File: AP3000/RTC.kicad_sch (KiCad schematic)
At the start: 10 parts, among them U14 74LVC1G07SE-7, U8 PCF85063AT/AAZ, Y2 X32K768S301

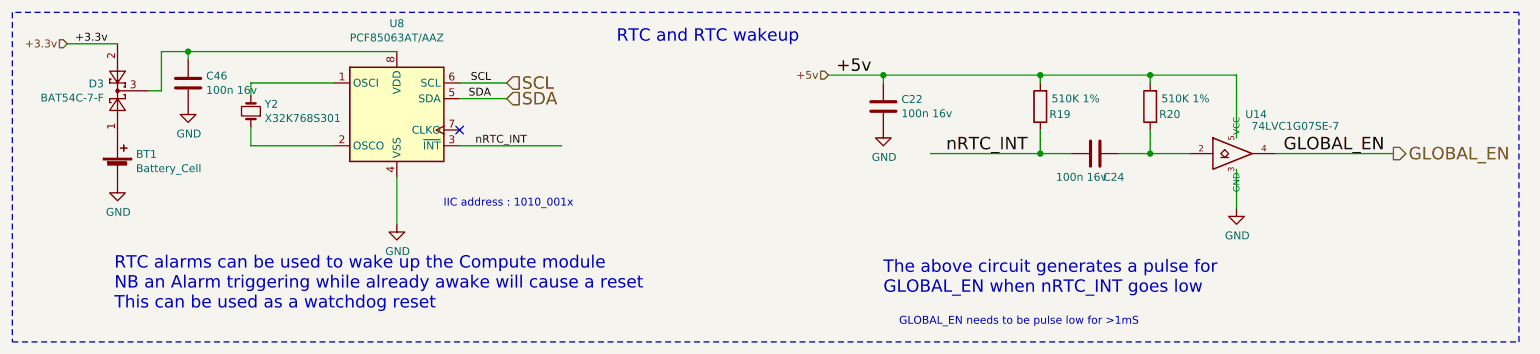
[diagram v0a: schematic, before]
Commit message: Update JLCPCB components for AP3000
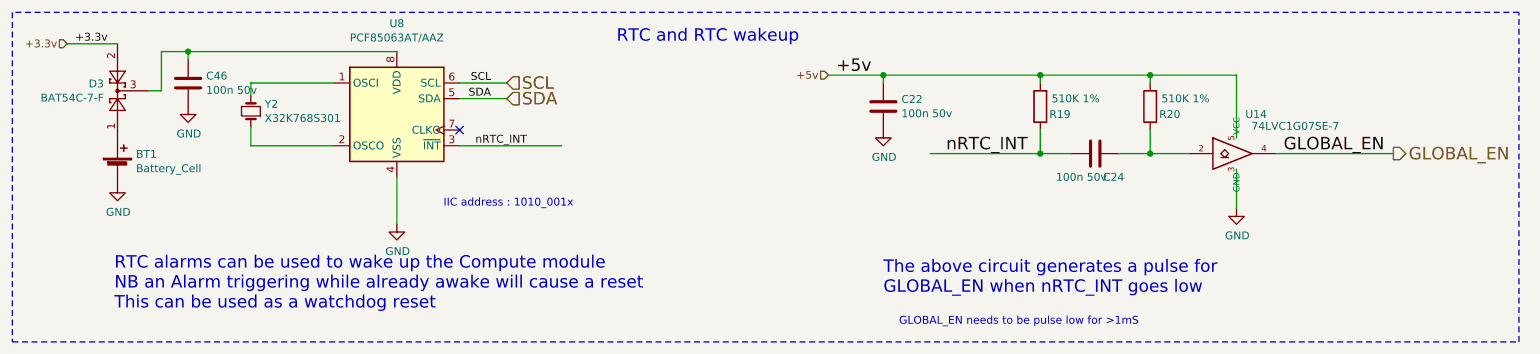
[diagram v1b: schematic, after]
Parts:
- BT1: Part Description Battery Retainer Coin, 20.0mm 1 Cell SMD (SMT) Tab -> Battery Retainer Coin, 20.0mm 1 Cell SMD (SMT) Tab
- C22, C24, C46: value 100n 16v -> 100n 50v; LCSC (none) -> C14663; Part Description 0.1uF 10% 16V Ceramic Capacitor X7R 0402 (1005 Metric) -> 100nF 10% or 20% 50V Ceramic Capacitor X7R 0603; PartsBoxID 0603-100nF-X7R-16V -> 0603-100nF-X7R-50V
- D3: LCSC (none) -> C134405
- R19, R20: LCSC (none) -> C23192
- U14: LCSC (none) -> C67531
- U8: LCSC (none) -> 2157792
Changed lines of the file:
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@@
       (effects (font (size 1.27 1.27)) hide)
     )
-    (property "PartsBoxID" "ABS07-32.768KHZ-7-T" (id 4) (at 67.818 55.372 0)
+    (property "PartsBoxID" "ABS07-32.768KHZ-7-T" (id 7) (at 67.818 55.372 0)
       (effects (font (size 1.27 1.27)) hide)
     )
@@
       (effects (font (size 1.27 1.27)) hide)
     )
-    (property "PartsBoxID" "0603-510K-1%" (id 4) (at 195.58 54.61 0)
+    (property "PartsBoxID" "0603-510K-1%" (id 9) (at 195.58 54.61 0)
+      (effects (font (size 1.27 1.27)) hide)
+    )
+    (property "LCSC" "C23192" (id 10) (at 195.58 54.61 0)
       (effects (font (size 1.27 1.27)) hide)
     )
@@
       (effects (font (size 1.27 1.27)) hide)
     )
-    (property "PartsBoxID" "0603-510K-1%" (id 4) (at 213.36 54.61 0)
+    (property "PartsBoxID" "0603-510K-1%" (id 9) (at 213.36 54.61 0)
+      (effects (font (size 1.27 1.27)) hide)
+    )
+    (property "LCSC" "C23192" (id 10) (at 213.36 54.61 0)
       (effects (font (size 1.27 1.27)) hide)
     )
@@
       (effects (font (size 1.27 1.27)) hide)
     )
-    (property "Part Description" "	Battery Retainer Coin, 20.0mm 1 Cell SMD (SMT) Tab" (id 8) (at 46.228 64.77 0)
-      (effects (font (size 1.27 1.27)) hide)
-    )
-    (property "PartsBoxID" "3034" (id 4) (at 46.228 64.77 0)
+    (property "Part Description" "Battery Retainer Coin, 20.0mm 1 Cell SMD (SMT) Tab" (id 8) (at 46.228 64.77 0)
+      (effects (font (size 1.27 1.27)) hide)
+    )
+    (property "PartsBoxID" "3034" (id 9) (at 46.228 64.77 0)
       (effects (font (size 1.27 1.27)) hide)
     )
@@
       (effects (font (size 1.27 1.27)) (justify left))
     )
-    (property "Value" "100n 16v" (id 1) (at 60.579 51.9684 0)
+    (property "Value" "100n 50v" (id 1) (at 60.579 51.9684 0)
       (effects (font (size 1.27 1.27)) (justify left))
     )
@@
       (effects (font (size 1.27 1.27)) hide)
     )
-    (property "Part Description" "	0.1uF 10% 16V Ceramic Capacitor X7R 0402 (1005 Metric)" (id 8) (at 57.658 50.8254 0)
+    (property "Part Description" "100nF 10% or 20% 50V Ceramic Capacitor X7R 0603" (id 8) (at 57.658 50.8254 0)
       (effects (font (size 1.27 1.27)) hide)
     )
@@
       (effects (font (size 1.27 1.27)) hide)
     )
-    (property "PartsBoxID" "0603-100nF-X7R-16V" (id 4) (at 57.658 50.8254 0)
+    (property "PartsBoxID" "0603-100nF-X7R-50V" (id 10) (at 57.658 50.8254 0)
+      (effects (font (size 1.27 1.27)) hide)
+    )
+    (property "LCSC" "C14663" (id 11) (at 57.658 50.8254 0)
       (effects (font (size 1.27 1.27)) hide)
     )
@@
       (effects (font (size 1.27 1.27)) (justify left))
     )
-    (property "Value" "100n 16v" (id 1) (at 173.101 55.753 0)
+    (property "Value" "100n 50v" (id 1) (at 173.101 55.753 0)
       (effects (font (size 1.27 1.27)) (justify left))
     )
@@
       (effects (font (size 1.27 1.27)) hide)
     )
-    (property "Part Description" "	0.1uF 10% 16V Ceramic Capacitor X7R 0402 (1005 Metric)" (id 8) (at 170.18 54.61 0)
+    (property "Part Description" "100nF 10% or 20% 50V Ceramic Capacitor X7R 0603" (id 8) (at 170.18 54.61 0)
       (effects (font (size 1.27 1.27)) hide)
     )
@@
       (effects (font (size 1.27 1.27)) hide)
     )
-    (property "PartsBoxID" "0603-100nF-X7R-16V" (id 4) (at 170.18 54.61 0)
+    (property "PartsBoxID" "0603-100nF-X7R-50V" (id 10) (at 170.18 54.61 0)
+      (effects (font (size 1.27 1.27)) hide)
+    )
+    (property "LCSC" "C14663" (id 11) (at 170.18 54.61 0)
       (effects (font (size 1.27 1.27)) hide)
     )
@@
       (effects (font (size 1.27 1.27)) (justify left))
     )
-    (property "Value" "100n 16v" (id 1) (at 198.12 66.04 90)
+    (property "Value" "100n 50v" (id 1) (at 198.12 66.04 90)
       (effects (font (size 1.27 1.27)) (justify left))
     )
@@
       (effects (font (size 1.27 1.27)) hide)
     )
-    (property "Part Description" "	0.1uF 10% 16V Ceramic Capacitor X7R 0402 (1005 Metric)" (id 8) (at 204.47 62.23 0)
+    (property "Part Description" "100nF 10% or 20% 50V Ceramic Capacitor X7R 0603" (id 8) (at 204.47 62.23 0)
       (effects (font (size 1.27 1.27)) hide)
     )
@@
       (effects (font (size 1.27 1.27)) hide)
     )
-    (property "PartsBoxID" "0603-100nF-X7R-16V" (id 4) (at 204.47 62.23 0)
-      (effects (font (size 1.27 1.27)) hide)
-    )
-    (pin "1")
-    (pin "2")
-  )
-  (symbol (lib_id "Diode:BAT54C") (at 46.228 52.07 90) (unit 1)
-    (in_bom yes) (on_board yes)
-    (property "Reference" "D3" (id 0) (at 44.0182 50.927 90)
-      (effects (font (size 1.27 1.27)) (justify left))
-    )
-    (property "Value" "BAT54C-7-F" (id 1) (at 44.0182 53.213 90)
-      (effects (font (size 1.27 1.27)) (justify left))
-    )
-    (property "Footprint" "Package_TO_SOT_SMD:SOT-23" (id 2) (at 43.053 50.165 0)
-      (effects (font (size 1.27 1.27)) (justify left) hide)
-    )
-    (property "Datasheet" "http://www.farnell.com/datasheets/2861240.pdf?_ga=2.129831176.54358802.1587372871-1787849031.1568210898&_gac=1.175311126.1587399424.EAIaIQobChMInOvF07P36AIVw7HtCh0NWwCeEAAYAyAAEgI0YfD_BwE" (id 3) (at 46.228 54.102 0)
-      (effects (font (size 1.27 1.27)) hide)
-    )
-    (property "Field4" "Farnell" (id 4) (at 46.228 52.07 0)
-      (effects (font (size 1.27 1.27)) hide)
-    )
-    (property "Field5" "2306010" (id 5) (at 46.228 52.07 0)
-      (effects (font (size 1.27 1.27)) hide)
-    )
-    (property "Field6" "BAT54C-7-F" (id 6) (at 46.228 52.07 0)
-      (effects (font (size 1.27 1.27)) hide)
-    )
-    (property "Field7" "Rohm" (id 7) (at 46.228 52.07 0)
-      (effects (font (size 1.27 1.27)) hide)
-    )
-    (property "Part Description" "Diode Array 1 Pair Common Cathode Schottky 30V 200mA (DC) Surface Mount TO-236-3, SC-59, SOT-23-3" (id 8) (at 46.228 52.07 0)
-      (effects (font (size 1.27 1.27)) hide)
-    )
-    (property "PartsBoxID" "BAT54C-7-F" (id 4) (at 46.228 52.07 0)
-      (effects (font (size 1.27 1.27)) hide)
-    )
-    (pin "1")
-    (pin "2")
-    (pin "3")
+    (property "PartsBoxID" "0603-100nF-X7R-50V" (id 10) (at 204.47 62.23 0)
+      (effects (font (size 1.27 1.27)) hide)
+    )
+    (property "LCSC" "C14663" (id 11) (at 204.47 62.23 0)
+      (effects (font (size 1.27 1.27)) hide)
+    )
+    (pin "1")
+    (pin "2")
   )
   (symbol (lib_id "AP3000:74LVC1G07_copy") (at 227.33 62.23 0) (unit 1)
@@
       (effects (font (size 1.27 1.27)) hide)
     )
-    (property "PartsBoxID" "74LVC1G07SE-7" (id 4) (at 227.33 62.23 0)
+    (property "PartsBoxID" "74LVC1G07SE-7" (id 9) (at 227.33 62.23 0)
+      (effects (font (size 1.27 1.27)) hide)
+    )
+    (property "LCSC" "C67531" (id 10) (at 227.33 62.23 0)
       (effects (font (size 1.27 1.27)) hide)
     )
@@
     (pin "5")
   )
+  (symbol (lib_id "Diode:BAT54C") (at 46.228 52.07 90) (unit 1)
+    (in_bom yes) (on_board yes)
+    (property "Reference" "D3" (id 0) (at 44.0182 50.927 90)
+      (effects (font (size 1.27 1.27)) (justify left))
+    )
+    (property "Value" "BAT54C-7-F" (id 1) (at 44.0182 53.213 90)
+      (effects (font (size 1.27 1.27)) (justify left))
+    )
+    (property "Footprint" "Package_TO_SOT_SMD:SOT-23" (id 2) (at 43.053 50.165 0)
+      (effects (font (size 1.27 1.27)) (justify left) hide)
+    )
+    (property "Datasheet" "http://www.farnell.com/datasheets/2861240.pdf?_ga=2.129831176.54358802.1587372871-1787849031.1568210898&_gac=1.175311126.1587399424.EAIaIQobChMInOvF07P36AIVw7HtCh0NWwCeEAAYAyAAEgI0YfD_BwE" (id 3) (at 46.228 54.102 0)
+      (effects (font (size 1.27 1.27)) hide)
+    )
+    (property "Field4" "Farnell" (id 4) (at 46.228 52.07 0)
+      (effects (font (size 1.27 1.27)) hide)
+    )
+    (property "Field5" "2306010" (id 5) (at 46.228 52.07 0)
+      (effects (font (size 1.27 1.27)) hide)
+    )
+    (property "Field6" "BAT54C-7-F" (id 6) (at 46.228 52.07 0)
+      (effects (font (size 1.27 1.27)) hide)
+    )
+    (property "Field7" "Rohm" (id 7) (at 46.228 52.07 0)
+      (effects (font (size 1.27 1.27)) hide)
+    )
+    (property "Part Description" "Diode Array 1 Pair Common Cathode Schottky 30V 200mA (DC) Surface Mount TO-236-3, SC-59, SOT-23-3" (id 8) (at 46.228 52.07 0)
+      (effects (font (size 1.27 1.27)) hide)
+    )
+    (property "PartsBoxID" "BAT54C-7-F" (id 9) (at 46.228 52.07 0)
+      (effects (font (size 1.27 1.27)) hide)
+    )
+    (property "LCSC" "C134405" (id 10) (at 46.228 52.07 0)
+      (effects (font (size 1.27 1.27)) hide)
+    )
+    (pin "1")
+    (pin "2")
+    (pin "3")
+  )
   (symbol (lib_id "Timer_RTC:PCF8563T") (at 91.44 55.88 0) (unit 1)
     (in_bom yes) (on_board yes)
@@
       (effects (font (size 1.27 1.27)) hide)
     )
-    (property "PartsBoxID" "PCF85063AT/AY" (id 4) (at 91.44 55.88 0)
-      (effects (font (size 1.27 1.27)) hide)
-    )
+    (property "PartsBoxID" "PCF85063AT/AY" (id 9) (at 91.44 55.88 0)
+      (effects (font (size 1.27 1.27)) hide)
+    )
+    (property "LCSC" "2157792" (id 10) (at 91.44 55.88 0)
+      (effects (font (size 1.27 1.27)) hide)
+    )

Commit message: Many enhancements to the AP3000 board. Reworking FlatAntPanel4x4 again with proper holes Made a connector test pcb
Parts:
- U8: LCSC 2157792 -> (none)
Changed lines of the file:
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@@
-(kicad_sch (version 20210126) (generator eeschema)
+(kicad_sch (version 20210406) (generator eeschema)
   (paper "A4")
   (title_block
@@
       (effects (font (size 1.27 1.27)) hide)
     )
-    (property "LCSC" "2157792" (id 10) (at 91.44 55.88 0)
-      (effects (font (size 1.27 1.27)) hide)
-    )
+    (property "LCSC" "" (id 10) (at 91.44 55.88 0)
+      (effects (font (size 1.27 1.27)) hide)
+    )

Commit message: Updates for JLCPCB components actually in stock at this time
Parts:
- U14: footprint Package_TO_SOT_SMD:SOT-353_SC-70-5 -> Package_TO_SOT_SMD:SOT-23-5; LCSC C67531 -> C7829
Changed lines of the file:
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@@
     (property "Reference" "U14" (id 0) (at 230.505 55.88 0))
     (property "Value" "74LVC1G07SE-7" (id 1) (at 236.855 57.785 0))
-    (property "Footprint" "Package_TO_SOT_SMD:SOT-353_SC-70-5" (id 2) (at 227.33 62.23 0)
+    (property "Footprint" "Package_TO_SOT_SMD:SOT-23-5" (id 2) (at 227.33 62.23 0)
       (effects (font (size 1.27 1.27)) hide)
     )
@@
       (effects (font (size 1.27 1.27)) hide)
     )
-    (property "LCSC" "C67531" (id 10) (at 227.33 62.23 0)
+    (property "LCSC" "C7829" (id 10) (at 227.33 62.23 0)
       (effects (font (size 1.27 1.27)) hide)
     )
